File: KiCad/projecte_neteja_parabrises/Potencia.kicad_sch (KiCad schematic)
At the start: 19 parts, among them K1 G6K-2, K3 Fujitsu_FTR-LYAA005x, M1 Motor_DC, M2 Motor_DC, M3 Motor_DC, M4 Motor_DC, Q1 MMBT3904, Q3 MMBT3904, U3 DRV8871DDA, U4 DRV8871DDA

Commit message: potencia cambios
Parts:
- added FB1: FerriteBead, symbol Device:FerriteBead
- added R18: 7.6k, Resistor_SMD:R_0603_1608Metric_Pad0.98x0.95mm_HandSolder, symbol Device:R
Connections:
- net GND: now also FB1.2, R18.2
- net at Q3.1 (B), R4.2: now also R18.1
- new net GND_PWR: FB1.1
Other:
- moved on the sheet: R4

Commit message: POTENCIA GND
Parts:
- removed D1: D, Diode_SMD:D_0201_0603Metric_Pad0.64x0.40mm_HandSolder, symbol Device:D
- removed K1: G6K-2, Relay_THT:Relay_DPDT_Omron_G6K-2P, symbol Relay:G6K-2
- removed M4: Motor_DC, TerminalBlock:TerminalBlock_MaiXu_MX126-5.0-02P_1x02_P5.00mm, symbol Motor:Motor_DC
- removed Q1: MMBT3904, Package_TO_SOT_SMD:SOT-23, symbol Transistor_BJT:MMBT3904
- removed R1: 4.7K, Resistor_SMD:R_0603_1608Metric_Pad0.98x0.95mm_HandSolder, symbol Device:R
- removed U4: DRV8871DDA, Package_SO:Texas_HTSOP-8-1EP_3.9x4.9mm_P1.27mm_EP2.95x4.9mm_Mask2.4x3.1mm_ThermalVias, symbol Driver_Motor:DRV8871DDA
- added D5, D6: D, Diode_SMD:D_0201_0603Metric_Pad0.64x0.40mm_HandSolder, symbol Device:D
- added K2, K4: Fujitsu_FTR-LYAA005x, Relay_THT:Relay_SPST-NO_Fujitsu_FTR-LYAA005x_FormA_Vertical, symbol Relay:Fujitsu_FTR-LYAA005x
- added M5: Motor_DC, TerminalBlock:TerminalBlock_MaiXu_MX126-5.0-02P_1x02_P5.00mm, symbol Motor:Motor_DC
- added Q2, Q4: MMBT3904, Package_TO_SOT_SMD:SOT-23, symbol Transistor_BJT:MMBT3904
- added R13, R14: 4.7K, Resistor_SMD:R_0603_1608Metric_Pad0.98x0.95mm_HandSolder, symbol Device:R
- added R22, R23: 7.6k, Resistor_SMD:R_0603_1608Metric_Pad0.98x0.95mm_HandSolder, symbol Device:R
- added U7: DRV8871DDA, Package_SO:Texas_HTSOP-8-1EP_3.9x4.9mm_P1.27mm_EP2.95x4.9mm_Mask2.4x3.1mm_ThermalVias, symbol Driver_Motor:DRV8871DDA
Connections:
- net 12V: now also D5.1 (K), D6.1 (K), K2.13, K2.A1, K4.13, K4.A1, U7.5 (VM)
- net GATE B: now also R13.1, R14.1
- net GND: now also Q2.2 (E), Q4.2 (E), R22.2, R23.2, U7.2 (IN2); no longer M3.2 (-), R11.2, U3.1 (GND), U3.7 (GND), U3.9 (GND)
- net GND_PWR: now also M3.2 (-), U3.1 (GND), U3.7 (GND), U3.9 (GND), M5.2 (-), U7.1 (GND), U7.7 (GND), U7.9 (GND)
- net PWM: now also U7.3 (IN1)
- net at M1.1 (+): now also U7.6 (OUT1)
- net at M1.2 (-): now also U7.8 (OUT2)
- net at M3.1 (+): now also K4.14
- new net: Q4.1 (B), R14.2, R23.1
- new net: D6.2 (A), K2.A2, Q4.3 (C)
- new net: Q2.1 (B), R13.2, R22.1
- new net: D5.2 (A), K4.A2, Q2.3 (C)
- new net: K2.14, M5.1 (+)
- no-connect marks 6 -> 4
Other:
- moved on the sheet: M2, M3, U3

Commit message: huella ferrita
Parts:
- FB1: footprint (none) -> Ferrite_THT:LairdTech_28C0236-0JW-10
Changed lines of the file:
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@@
 			)
 		)
-		(property "Footprint" ""
+		(property "Footprint" "Ferrite_THT:LairdTech_28C0236-0JW-10"
 			(at 139.7 128.778 90)
 			(effects

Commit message: Pines
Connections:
- net GATE B: no longer R13.1
- new net GATE B2: R13.1
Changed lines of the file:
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@@
 		)
 	)
-	(global_label "GATE B"
+	(global_label "GATE B2"
 		(shape input)
 		(at 140.208 74.676 180)
@@
 		)
 		(property "Intersheetrefs" "${INTERSHEET_REFS}"
-			(at 130.51 74.676 0)
+			(at 129.3005 74.676 0)
 			(effects
 				(font

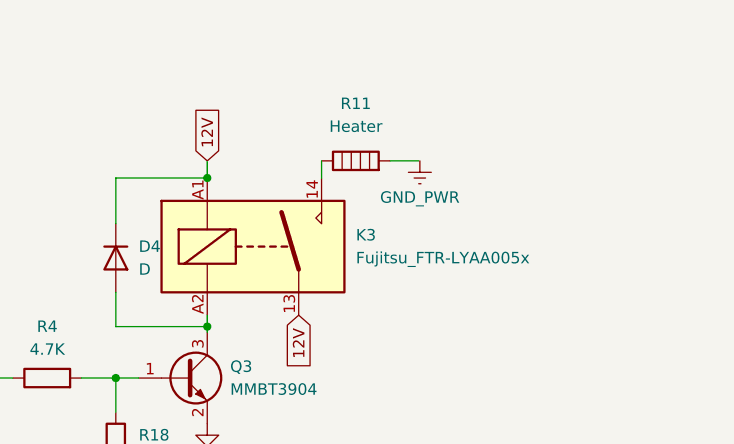
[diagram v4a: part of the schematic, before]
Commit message: pcb placement
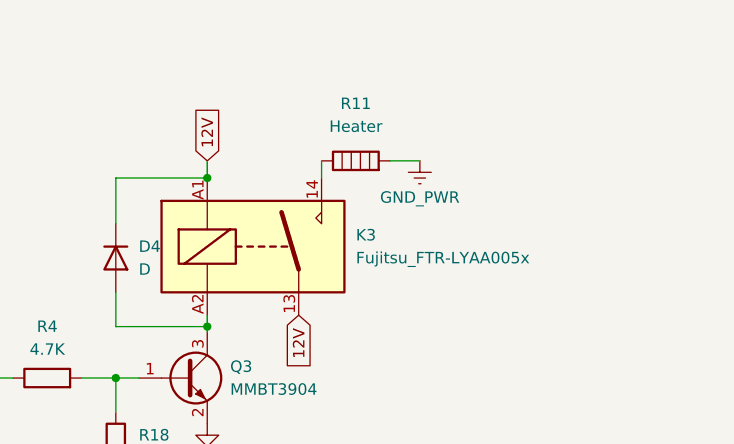
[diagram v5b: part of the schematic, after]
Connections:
- net GND_PWR: now also R11.2
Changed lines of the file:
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@@
+	(wire
+		(pts
+			(xy 248.92 27.94) (xy 252.222 27.94)
+		)
+		(stroke
+			(width 0)
+			(type default)
+		)
+	)
 	(wire
 		(pts
@@
 		)
 		(stroke
-			(width 0)
-			(type default)
-		)
-	)
-	(wire
-		(pts
-			(xy 252.095 27.94) (xy 248.92 27.94)
-		)
-		(stroke

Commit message: pcb
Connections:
- net VCC renamed VDD
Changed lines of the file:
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@@
 		)
 	)
-	(global_label "VCC"
+	(global_label "VDD"
 		(shape input)
 		(at 42.545 99.06 90)
@@
 		)
 	)
-	(global_label "VCC"
+	(global_label "VDD"
 		(shape input)
 		(at 42.545 118.11 90)
